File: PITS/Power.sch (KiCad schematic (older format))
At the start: 5 parts, among them Q1 Q_PMOS_DGS, Q2 Q_PNP_dual, U5 TPS61030

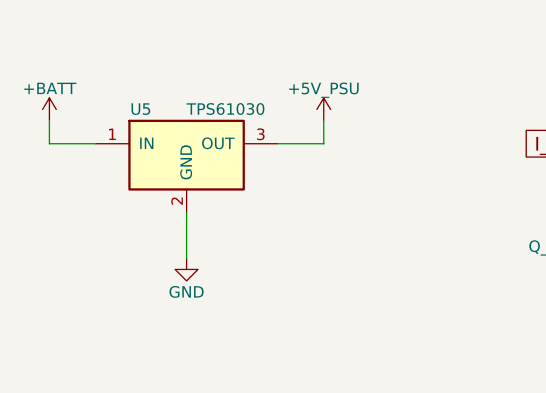
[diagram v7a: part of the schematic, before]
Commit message: Fix #8 & #9
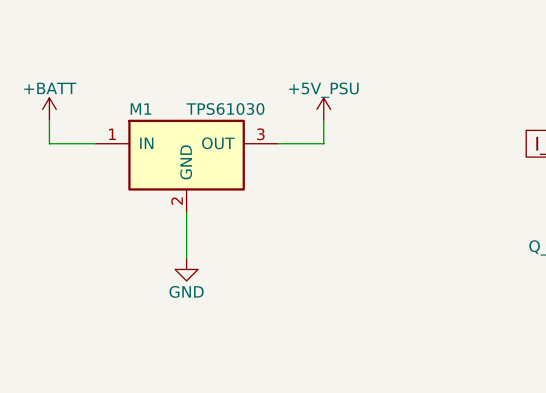
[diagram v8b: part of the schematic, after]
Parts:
- renumbered U5 to M1
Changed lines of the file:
@@
 $EndComp
 $Comp
-L LM7805CT U5
+L LM7805CT M1
 U 1 1 598E0500
 P 4400 3250
-F 0 "U5" H 4200 3450 50  0000 C CNN
+F 0 "M1" H 4200 3450 50  0000 C CNN
 F 1 "TPS61030" H 4400 3450 50  0000 L CNN
 F 2 "power:TPS61030" H 4400 3350 50  0001 C CIN
